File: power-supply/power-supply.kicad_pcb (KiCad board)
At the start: 2 copper layers, 25.4 x 25.4 mm, 12 parts, among them J1 Conn_01x04, Q1 Q_PMOS_GSD, Q3 Q_NMOS_GSD, U1 AZ1084-5.0

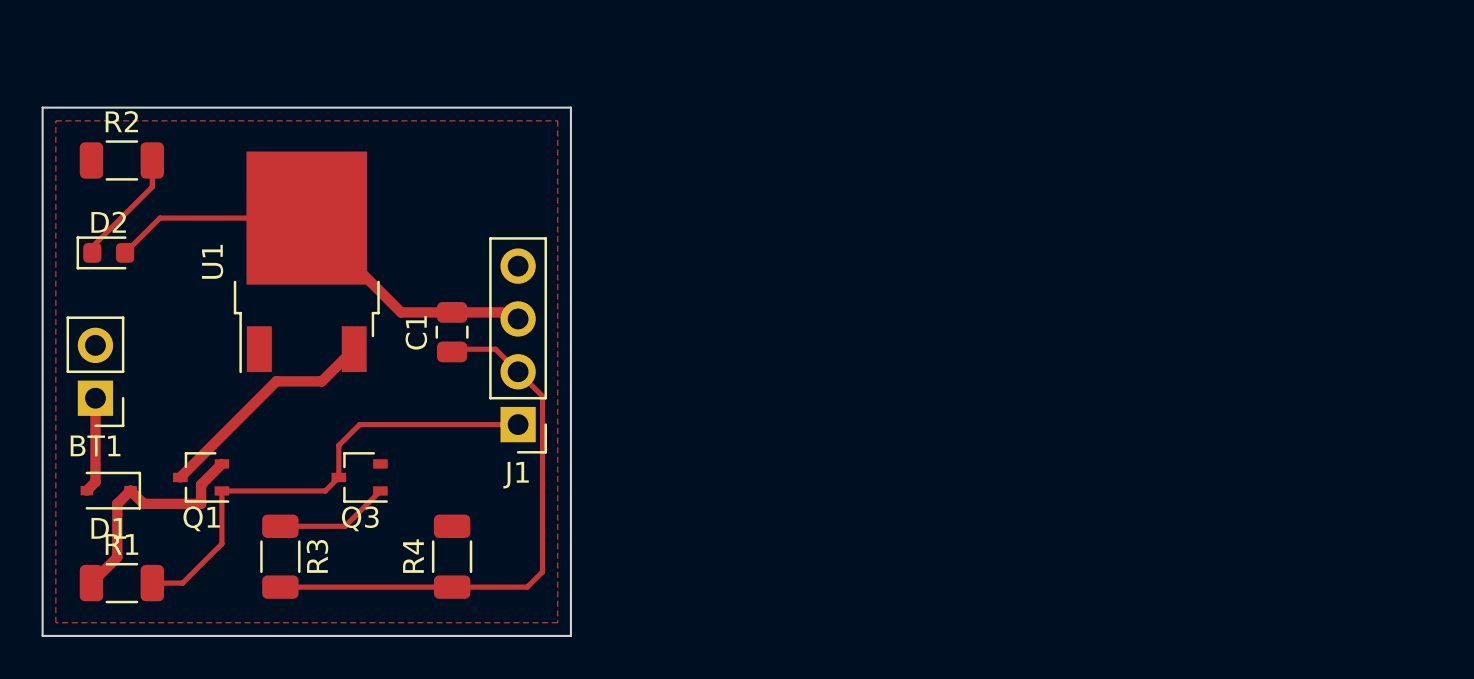
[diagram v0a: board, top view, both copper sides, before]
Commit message: Rearranged onto a smaller board
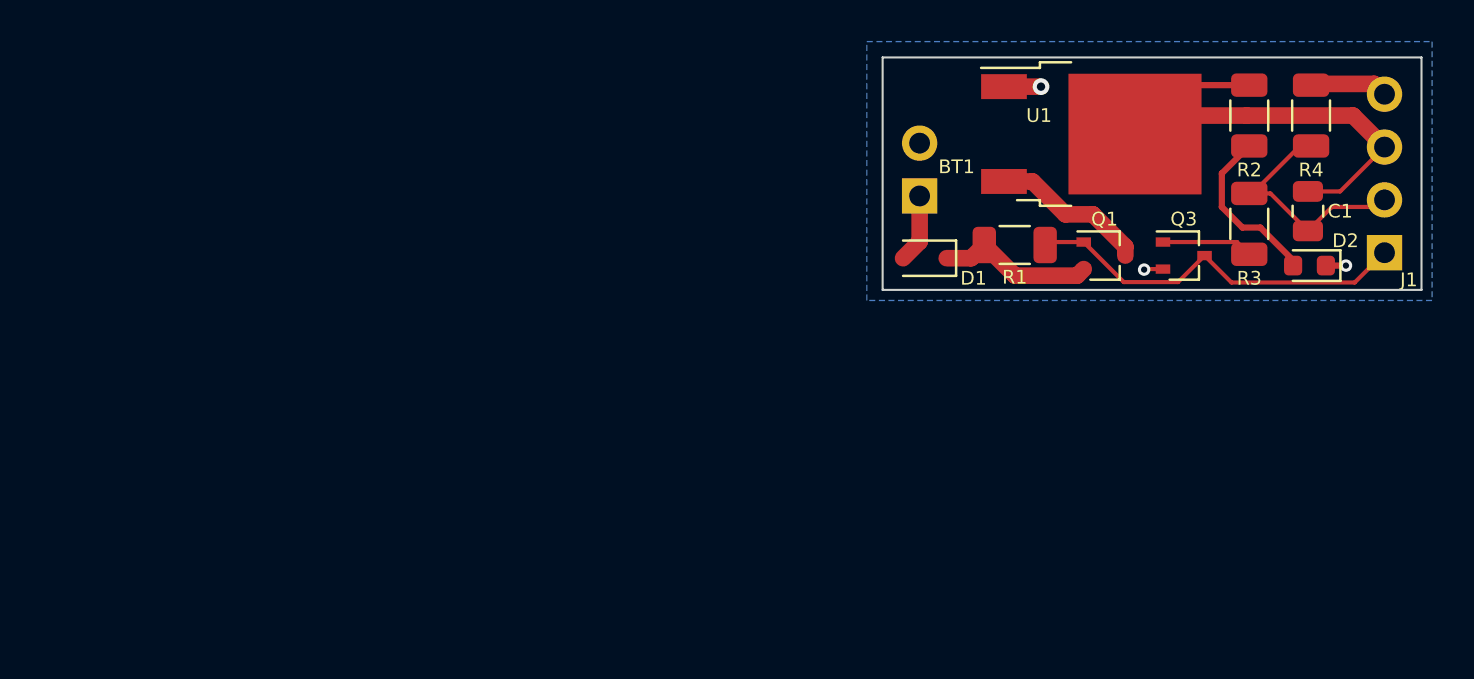
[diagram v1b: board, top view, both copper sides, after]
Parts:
- D2: value LED (LEDC1608X80N) -> LED (LEDC1608X80N) (150060VS75000)
- moved D2 57.7 mm to (106.6, 83.2), turned to 180 degrees
- moved R2 54.2 mm to (103.7, 75.9), turned to 90 degrees
- moved R3 49.3 mm to (103.7, 81.2), turned to 90 degrees
- moved R4 46.4 mm to (106.7, 75.9)
- moved R1 45.9 mm to (92.5, 82.2)
- moved Q1 44.7 mm to (96.8, 82.7), turned to 0 degrees
- moved J1 42.5 mm to (110.2, 82.5)
- moved C1 41.6 mm to (106.6, 80.5)
- moved Q3 41.0 mm to (100.6, 82.7), turned to 0 degrees
- moved D1 40.8 mm to (88.1, 82.8)
- moved BT1 40.8 mm to (87.9, 79.8)
- moved U1 38.2 mm to (96.1, 76.8), turned to 0 degrees
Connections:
- D2 pad 1: Net-(D2-Pad1) -> GND
- D2 pad 2: Net-(C1-Pad2) -> Net-(R2-Pad1)
- R2 pad 1: GND -> Net-(R2-Pad1)
- R2 pad 2: Net-(D2-Pad1) -> Net-(C1-Pad2)
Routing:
- net Net-(C1-Pad1): track 26.6 -> 11.8 mm
- net Net-(R2-Pad1): track 0.00 -> 8.22 mm
- net GND: track 0.00 -> 7.42 mm, vias 0 -> 3
- net Net-(D2-Pad1): track 5.62 -> 0.00 mm
- net Net-(J1-Pad1): track 23.1 -> 18.8 mm
- net Net-(D1-Pad1): track 11.2 -> 7.59 mm
- net Net-(Q1-Pad3): track 10.9 -> 7.56 mm
- net Net-(C1-Pad2): track 22.2 -> 24.0 mm
- net Net-(BT1-Pad1): track 4.62 -> 3.32 mm
- net Net-(Q3-Pad1): track 5.51 -> 4.39 mm
- added copper zone on B.Cu, net GND
- removed copper zone on F.Cu, net GND
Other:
- board size 25.4 x 25.4 mm -> 25.9 x 11.2 mm
- board text added: "5V"
- board text added: "GND"
- board text added: "KA"
- board text added: "TR"

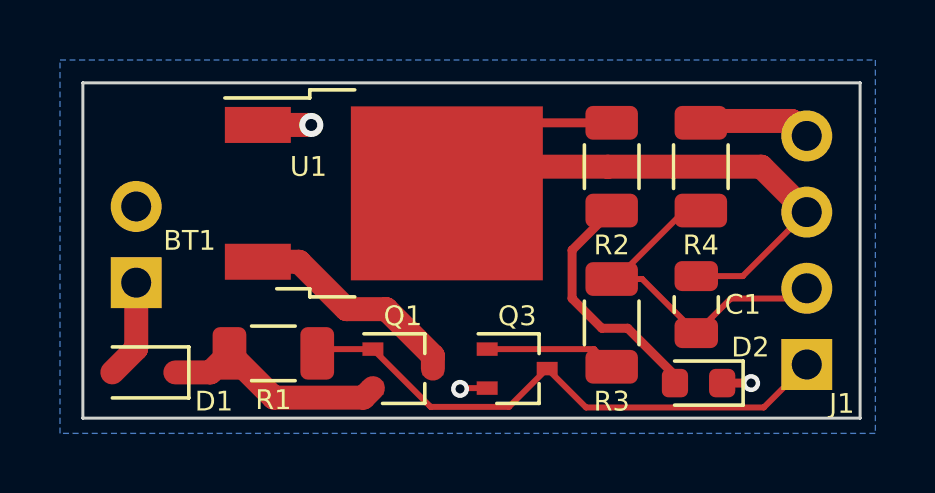
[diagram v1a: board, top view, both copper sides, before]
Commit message: decreased width to slightly under 25mm
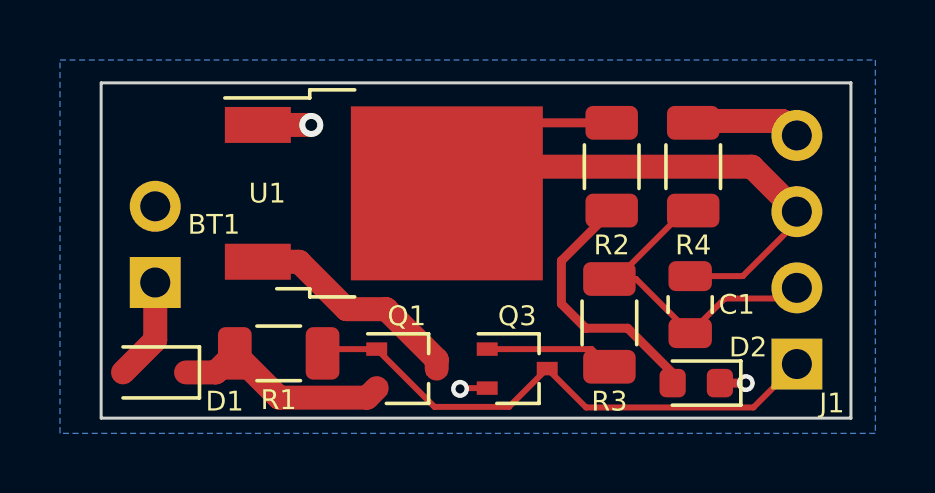
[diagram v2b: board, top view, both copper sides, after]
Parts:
- moved BT1 0.64 mm to (88.5, 79.8)
- moved D1 0.36 mm to (88.5, 82.8)
- moved J1 0.33 mm to (109.9, 82.5)
- moved R4 0.25 mm to (106.5, 75.9)
- moved C1 0.20 mm to (106.3, 80.5)
- moved R1 0.18 mm to (92.6, 82.2)
- moved Q1 0.13 mm to (96.9, 82.7)
- moved D2 0.08 mm to (106.6, 83.2)
- moved R3 0.08 mm to (103.7, 81.2)
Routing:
- net Net-(R2-Pad1): track 8.22 -> 8.80 mm
- net Net-(J1-Pad1): track 18.8 -> 18.3 mm
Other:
- board size 25.9 x 11.2 mm -> 25 x 11.2 mm

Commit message: misc
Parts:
- moved R3 0.15 mm to (103.7, 81.0)
- moved C1 0.14 mm to (106.5, 80.4)
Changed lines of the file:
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@@
   )
   (footprint "Resistor_SMD:R_1206_3216Metric" (layer "F.Cu")
-    (at 103.6574 81.153 90)
+    (at 103.7336 81.026 90)
     (descr "Resistor SMD 1206 (3216 Metric), square (rectangular) end terminal, IPC_7351 nominal, (Body size source: IPC-SM-782 page 72, https://www.pcb-3d.com/wordpress/wp-content/uploads/ipc-sm-782a_amendment_1_and_2.pdf), generated with kicad-footprint-generator")
     (tags "resistor")
@@
   )
   (footprint "Capacitor_SMD:C_0805_2012Metric" (layer "F.Cu")
-    (at 106.3498 80.5434 90)
+    (at 106.4514 80.4418 90)
     (descr "Capacitor SMD 0805 (2012 Metric), square (rectangular) end terminal, IPC_7351 nominal, (Body size source: IPC-SM-782 page 76, https://www.pcb-3d.com/wordpress/wp-content/uploads/ipc-sm-782a_amendment_1_and_2.pdf, https://docs.google.com/spreadsheets/d/1BsfQQcO9C6DZCsRaXUlFlo91Tg2WpOkGARC1WS5S8t0/edit?usp=sharing), generated with kicad-footprint-generator")
     (tags "capacitor")
@@
     (style (thickness 0.1) (arrow_length 1.27) (text_position_mode 0) (extension_height 0.58642) (extension_offset 0.5) keep_text_aligned)
   )
-  (segment (start 106.3498 81.4934) (end 107.503 80.3402) (width 0.2) (layer "F.Cu") (net 1))
-  (segment (start 103.6574 79.6905) (end 104.5469 79.6905) (width 0.2) (layer "F.Cu") (net 1))
-  (segment (start 103.886 79.6905) (end 103.6574 79.6905) (width 0.2) (layer "F.Cu") (net 1))
-  (segment (start 106.168 77.4085) (end 103.886 79.6905) (width 0.2) (layer "F.Cu") (net 1))
+  (segment (start 103.7336 79.5635) (end 104.6231 79.5635) (width 0.2) (layer "F.Cu") (net 1))
+  (segment (start 106.4514 77.4085) (end 106.168 77.4085) (width 0.2) (layer "F.Cu") (net 1))
   (segment (start 109.5502 80.3402) (end 109.9058 79.9846) (width 0.2) (layer "F.Cu") (net 1))
-  (segment (start 104.5469 79.6905) (end 106.3498 81.4934) (width 0.2) (layer "F.Cu") (net 1))
-  (segment (start 106.4514 77.4085) (end 106.168 77.4085) (width 0.2) (layer "F.Cu") (net 1))
+  (segment (start 104.013 79.5635) (end 103.7336 79.5635) (width 0.2) (layer "F.Cu") (net 1))
   (segment (start 107.503 80.3402) (end 109.5502 80.3402) (width 0.2) (layer "F.Cu") (net 1))
+  (segment (start 106.4514 81.3918) (end 107.503 80.3402) (width 0.2) (layer "F.Cu") (net 1))
+  (segment (start 104.6231 79.5635) (end 106.4514 81.3918) (width 0.2) (layer "F.Cu") (net 1))
+  (segment (start 106.168 77.4085) (end 104.013 79.5635) (width 0.2) (layer "F.Cu") (net 1))
+  (segment (start 108.2042 79.4918) (end 109.9058 77.7902) (width 0.2) (layer "F.Cu") (net 2))
   (segment (start 99.128 75.946) (end 108.4072 75.946) (width 0.8) (layer "F.Cu") (net 2))
   (segment (start 100.5905 74.4835) (end 98.239 76.835) (width 0.3) (layer "F.Cu") (net 2))
   (segment (start 109.9058 77.7902) (end 109.9058 77.4446) (width 0.2) (layer "F.Cu") (net 2))
   (segment (start 98.239 76.835) (end 99.128 75.946) (width 0.8) (layer "F.Cu") (net 2))
-  (segment (start 106.3498 79.5934) (end 108.1026 79.5934) (width 0.2) (layer "F.Cu") (net 2))
+  (segment (start 106.4514 79.4918) (end 108.2042 79.4918) (width 0.2) (layer "F.Cu") (net 2))
   (segment (start 108.4072 75.946) (end 109.9058 77.4446) (width 0.8) (layer "F.Cu") (net 2))
-  (segment (start 108.1026 79.5934) (end 109.9058 77.7902) (width 0.2) (layer "F.Cu") (net 2))
   (segment (start 103.7336 74.4835) (end 100.5905 74.4835) (width 0.3) (layer "F.Cu") (net 2))
   (segment (start 95.584 83.644) (end 95.901 83.327) (width 0.8) (layer "F.Cu") (net 3))
@@
   (segment (start 88.519 79.8068) (end 88.519 81.7286) (width 0.8) (layer "F.Cu") (net 7))
   (segment (start 88.519 81.7286) (end 87.4436 82.804) (width 0.8) (layer "F.Cu") (net 7))
-  (segment (start 99.584 82.027) (end 103.0689 82.027) (width 0.2) (layer "F.Cu") (net 8))
-  (segment (start 103.0689 82.027) (end 103.6574 82.6155) (width 0.2) (layer "F.Cu") (net 8))
-  (segment (start 104.267 81.3308) (end 105.7655 82.8293) (width 0.3) (layer "F.Cu") (net 9))
-  (segment (start 102.87 81.3308) (end 104.267 81.3308) (width 0.3) (layer "F.Cu") (net 9))
+  (segment (start 103.2721 82.027) (end 103.7336 82.4885) (width 0.2) (layer "F.Cu") (net 8))
+  (segment (start 99.584 82.027) (end 103.2721 82.027) (width 0.2) (layer "F.Cu") (net 8))
   (segment (start 102.0572 79.0849) (end 102.0572 80.518) (width 0.3) (layer "F.Cu") (net 9))
+  (segment (start 105.3764 81.856) (end 105.3764 82.7705) (width 0.3) (layer "F.Cu") (net 9))
+  (segment (start 105.3764 82.7705) (end 105.7655 83.1596) (width 0.3) (layer "F.Cu") (net 9))
+  (segment (start 104.8512 81.3308) (end 105.3764 81.856) (width 0.3) (layer "F.Cu") (net 9))
+  (segment (start 103.7336 77.4085) (end 102.0572 79.0849) (width 0.3) (layer "F.Cu") (net 9))
+  (segment (start 102.87 81.3308) (end 104.8512 81.3308) (width 0.3) (layer "F.Cu") (net 9))
   (segment (start 102.0572 80.518) (end 102.87 81.3308) (width 0.3) (layer "F.Cu") (net 9))
-  (segment (start 103.7336 77.4085) (end 102.0572 79.0849) (width 0.3) (layer "F.Cu") (net 9))
-  (segment (start 105.7655 82.8293) (end 105.7655 83.1596) (width 0.3) (layer "F.Cu") (net 9))
   (zone (net 6) (net_name "GND") (layer "B.Cu") (hatch edge 0.508)
     (connect_pads (clearance 0.508))
